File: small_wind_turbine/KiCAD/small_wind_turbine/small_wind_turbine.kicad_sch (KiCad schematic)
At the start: 93 parts, among them J1 Conn_01x03_Male, J2 Conn_01x03_Male, J3 Conn_01x03_Male, J4 Conn_01x03_Male, K1 G5LE-1, Q1 Q_NMOS_GDS, SW1 SW_Push_SPDT, U10 AZ1117-5.0, U2 UC2844A, U3 LTC4440ES6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

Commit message: fix Q1 pin ordering
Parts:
- Q1: value Q_NMOS_GDS -> Q_NMOS_GSD; symbol Device:Q_NMOS_DGS -> Device:Q_NMOS_GSD
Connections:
- net GND: now also Q1.2 (S); no longer Q1.1 (D)
- net RELAY_DRIVE: now also Q1.1 (G); no longer Q1.2 (G)
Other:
- moved on the sheet: Q1
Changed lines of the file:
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@@
     (pin "3")
   )
-  (symbol (lib_id "Device:Q_NMOS_DGS") (at 134.62 31.75 270) (unit 1)
-    (in_bom yes) (on_board yes)
-    (property "Reference" "Q1" (id 0) (at 142.24 32.385 90))
-    (property "Value" "Q_NMOS_GDS" (id 1) (at 144.145 29.845 90))
-    (property "Footprint" "Package_TO_SOT_SMD:SOT-23" (id 2) (at 137.16 36.83 0)
-      (effects (font (size 1.27 1.27)) hide)
-    )
-    (property "Datasheet" "https://fscdn.rohm.com/en/products/databook/datasheet/discrete/transistor/mosfet/ruc002n05t116-e.pdf" (id 3) (at 134.62 31.75 0)
+  (symbol (lib_id "Device:Q_NMOS_GSD") (at 134.62 31.75 90) (mirror x) (unit 1)
+    (in_bom yes) (on_board yes)
+    (property "Reference" "Q1" (id 0) (at 127 32.385 90))
+    (property "Value" "Q_NMOS_GSD" (id 1) (at 149.86 30.48 90)
+      (effects (font (size 1.27 1.27)) (justify left))
+    )
+    (property "Footprint" "Package_TO_SOT_SMD:SOT-23" (id 2) (at 132.08 36.83 0)
+      (effects (font (size 1.27 1.27)) hide)
+    )
+    (property "Datasheet" "~" (id 3) (at 134.62 31.75 0)
       (effects (font (size 1.27 1.27)) hide)
     )
@@
     )
     (path "/118b0b0a-fa12-4ca4-b47b-2d44da30678e"
-      (reference "Q1") (unit 1) (value "Q_NMOS_GDS") (footprint "Package_TO_SOT_SMD:SOT-23")
+      (reference "Q1") (unit 1) (value "Q_NMOS_GSD") (footprint "Package_TO_SOT_SMD:SOT-23")
     )
     (path "/d52ff71e-c34a-4422-b42d-42d802a84e8c"

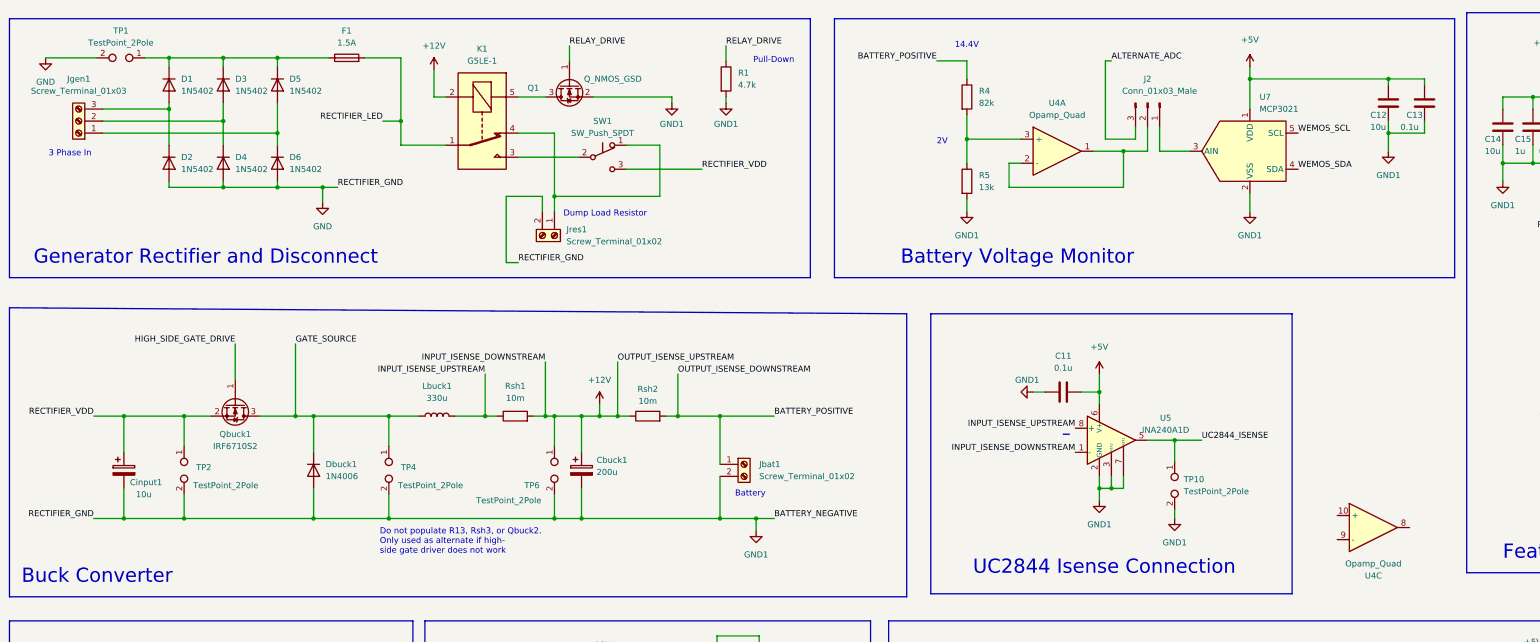
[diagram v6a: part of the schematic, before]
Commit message: add optional fuse terminal block
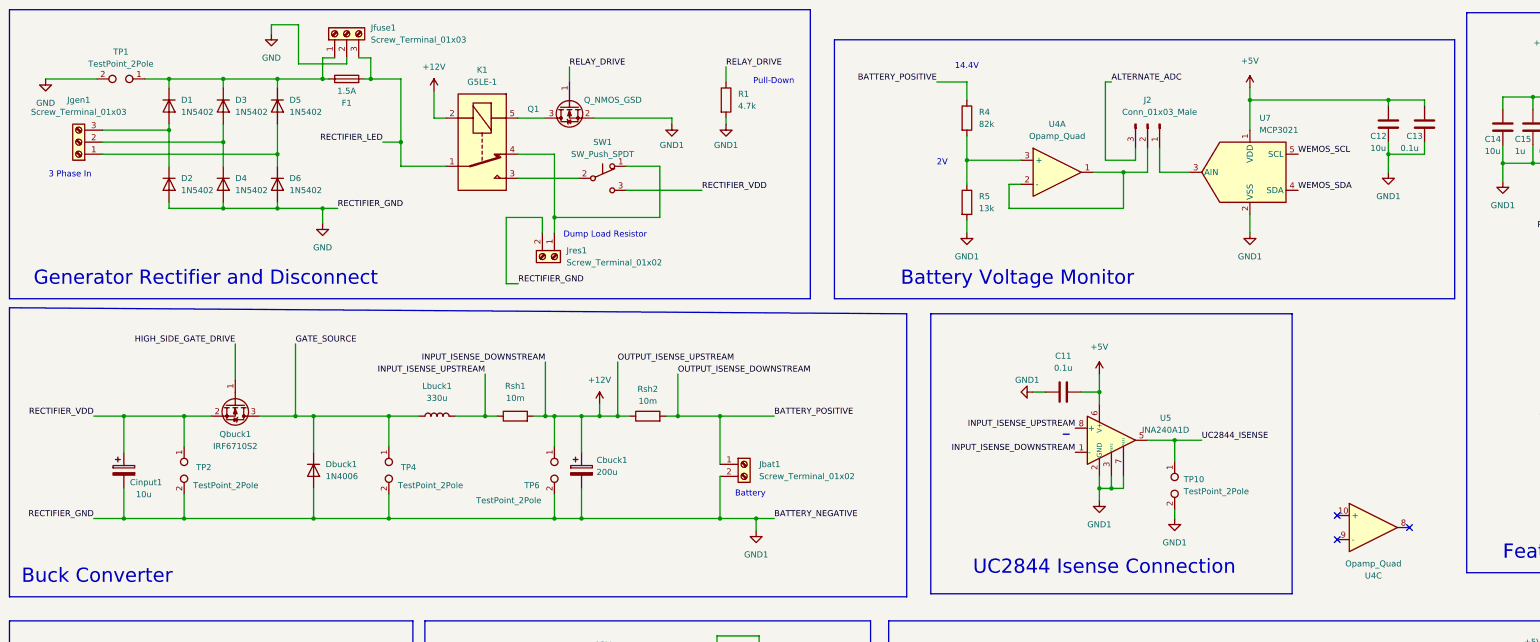
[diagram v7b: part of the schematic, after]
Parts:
- added Jfuse1: Screw_Terminal_01x03, small_wind_turbine:CUI_TBP01R1-508-03BE_no_extra, symbol Connector:Screw_Terminal_01x03
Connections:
- net GND: now also Jfuse1.2 (Pin_2)
- net RECTIFIER_LED: now also Jfuse1.3 (Pin_3)
- net at D1.1 (K), D3.1 (K), D5.1 (K)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: now also Jfuse1.1 (Pin_1)
- no-connect marks 16 -> 19
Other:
- note removed: "Do not populate R13, Rsh3, or Qbuck2. Only used as alternate if high- side gate driver does not work"
- moved on the sheet: C12, C13, D1, D2, D3, D4, D5, D6, F1, J2, Jgen1, Jres1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

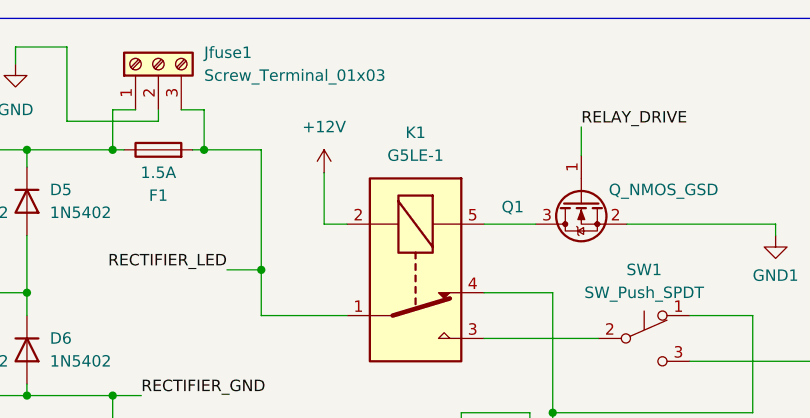
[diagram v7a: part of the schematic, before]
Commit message: add relay protection flyback diode
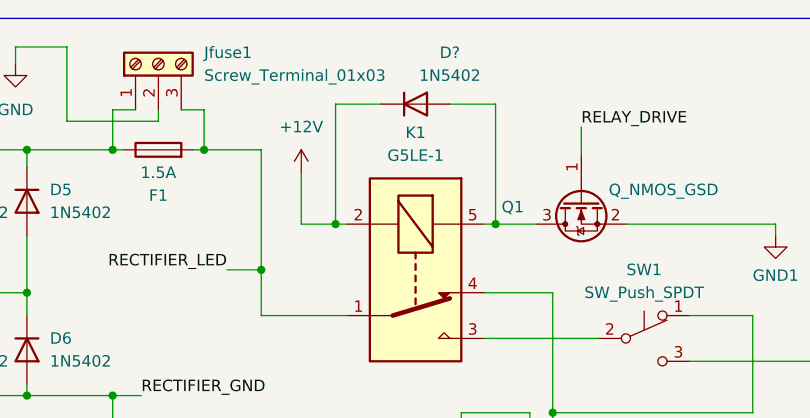
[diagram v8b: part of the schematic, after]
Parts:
- added D?: 1N5402, small_wind_turbine:SOD-323-EP_custom, symbol Diode:1N5402
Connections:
- net +12V: now also D?.1 (K)
- net at K1.5, Q1.3 (D): now also D?.2 (A)
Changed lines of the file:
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@@
   (junction (at 157.48 101.6) (diameter 0) (color 0 0 0 0)
   )
+  (junction (at 107.315 38.735) (diameter 0) (color 0 0 0 0)
+  )
   (junction (at 287.02 193.04) (diameter 0) (color 0 0 0 0)
   )
@@
   (junction (at 73.025 57.785) (diameter 0) (color 0 0 0 0)
   )
+  (junction (at 125.095 38.735) (diameter 0) (color 0 0 0 0)
+  )
   (junction (at 389.89 198.12) (diameter 0) (color 0 0 0 0)
   )
@@
     (stroke (width 0) (type default) (color 0 0 0 0))
   )
+  (wire (pts (xy 107.315 25.4) (xy 107.315 38.735))
+    (stroke (width 0) (type default) (color 0 0 0 0))
+  )
   (wire (pts (xy 302.895 224.155) (xy 322.58 224.155))
     (stroke (width 0) (type default) (color 0 0 0 0))
@@
     (stroke (width 0) (type default) (color 0 0 0 0))
   )
-  (wire (pts (xy 106.045 33.02) (xy 106.045 38.735))
+  (wire (pts (xy 103.505 33.02) (xy 103.505 38.735))
     (stroke (width 0) (type default) (color 0 0 0 0))
   )
@@
     (stroke (width 0) (type default) (color 0 0 0 0))
   )
+  (wire (pts (xy 125.095 25.4) (xy 125.095 38.735))
+    (stroke (width 0) (type default) (color 0 0 0 0))
+  )
   (wire (pts (xy 302.895 222.885) (xy 302.895 224.155))
     (stroke (width 0) (type default) (color 0 0 0 0))
@@
     (stroke (width 0) (type default) (color 0 0 0 0))
   )
+  (wire (pts (xy 125.095 38.735) (xy 129.54 38.735))
+    (stroke (width 0) (type default) (color 0 0 0 0))
+  )
   (wire (pts (xy 34.29 101.6) (xy 40.64 101.6))
     (stroke (width 0) (type default) (color 0 0 0 0))
@@
     (stroke (width 0) (type default) (color 0 0 0 0))
   )
+  (wire (pts (xy 120.015 25.4) (xy 125.095 25.4))
+    (stroke (width 0) (type default) (color 0 0 0 0))
+  )
   (wire (pts (xy 278.13 59.055) (xy 278.13 62.865))
     (stroke (width 0) (type default) (color 0 0 0 0))
@@
     (stroke (width 0) (type default) (color 0 0 0 0))
   )
-  (wire (pts (xy 106.045 38.735) (xy 108.585 38.735))
+  (wire (pts (xy 103.505 38.735) (xy 107.315 38.735))
     (stroke (width 0) (type default) (color 0 0 0 0))
   )
@@
     (stroke (width 0) (type default) (color 0 0 0 0))
   )
+  (wire (pts (xy 107.315 38.735) (xy 108.585 38.735))
+    (stroke (width 0) (type default) (color 0 0 0 0))
+  )
   (wire (pts (xy 49.53 201.93) (xy 66.04 201.93))
     (stroke (width 0) (type default) (color 0 0 0 0))
@@
     (stroke (width 0) (type default) (color 0 0 0 0))
   )
+  (wire (pts (xy 112.395 25.4) (xy 107.315 25.4))
+    (stroke (width 0) (type default) (color 0 0 0 0))
+  )
   (wire (pts (xy 292.1 224.79) (xy 292.1 227.33))
     (stroke (width 0) (type default) (color 0 0 0 0))
@@
     (stroke (width 0) (type default) (color 0 0 0 0))
   )
-  (wire (pts (xy 123.825 38.735) (xy 129.54 38.735))
+  (wire (pts (xy 123.825 38.735) (xy 125.095 38.735))
     (stroke (width 0) (type default) (color 0 0 0 0))
   )
@@
     (pin "3")
   )
-  (symbol (lib_id "power:+12V") (at 106.045 33.02 0) (unit 1)
+  (symbol (lib_id "power:+12V") (at 103.505 33.02 0) (unit 1)
     (in_bom yes) (on_board yes) (fields_autoplaced)
-    (property "Reference" "#PWR046" (id 0) (at 106.045 36.83 0)
+    (property "Reference" "#PWR046" (id 0) (at 103.505 36.83 0)
       (effects (font (size 1.27 1.27)) hide)
     )
-    (property "Value" "+12V" (id 1) (at 106.045 27.94 0))
-    (property "Footprint" "" (id 2) (at 106.045 33.02 0)
+    (property "Value" "+12V" (id 1) (at 103.505 27.94 0))
+    (property "Footprint" "" (id 2) (at 103.505 33.02 0)
       (effects (font (size 1.27 1.27)) hide)
     )
-    (property "Datasheet" "" (id 3) (at 106.045 33.02 0)
+    (property "Datasheet" "" (id 3) (at 103.505 33.02 0)
       (effects (font (size 1.27 1.27)) hide)
     )
@@
     (pin "2")
   )
+  (symbol (lib_id "Diode:1N5402") (at 116.205 25.4 0) (unit 1)
+    (in_bom yes) (on_board yes)
+    (property "Reference" "D?" (id 0) (at 120.015 19.685 0))
+    (property "Value" "1N5402" (id 1) (at 120.015 22.225 0))
+    (property "Footprint" "small_wind_turbine:SOD-323-EP_custom" (id 2) (at 116.205 29.845 0)
+      (effects (font (size 1.27 1.27)) hide)
+    )
+    (property "Datasheet" "https://www.vishay.com/docs/87203/v8pm153.pdf" (id 3) (at 116.205 25.4 0)
+      (effects (font (size 1.27 1.27)) hide)
+    )
+    (pin "1")
+    (pin "2")
+  )
   (symbol (lib_id "power:GND1") (at 173.99 125.73 0) (unit 1)
     (in_bom yes) (on_board yes) (fields_autoplaced)
@@
       (reference "D12") (unit 1) (value "LED") (footprint "LED_SMD:LED_0603_1608Metric")
     )
+    (path "/a636d248-70a9-4398-8397-b79925cddbcc"
+      (reference "D?") (unit 1) (value "1N5402") (footprint "small_wind_turbine:SOD-323-EP_custom")
+    )
     (path "/bf998c1e-9851-457c-bda0-bbc76f45eb14"
